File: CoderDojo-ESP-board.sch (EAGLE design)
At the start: 17 parts, among them IC1 ESP-12E/F, IC2 FT232RL, X1 PN61729-S

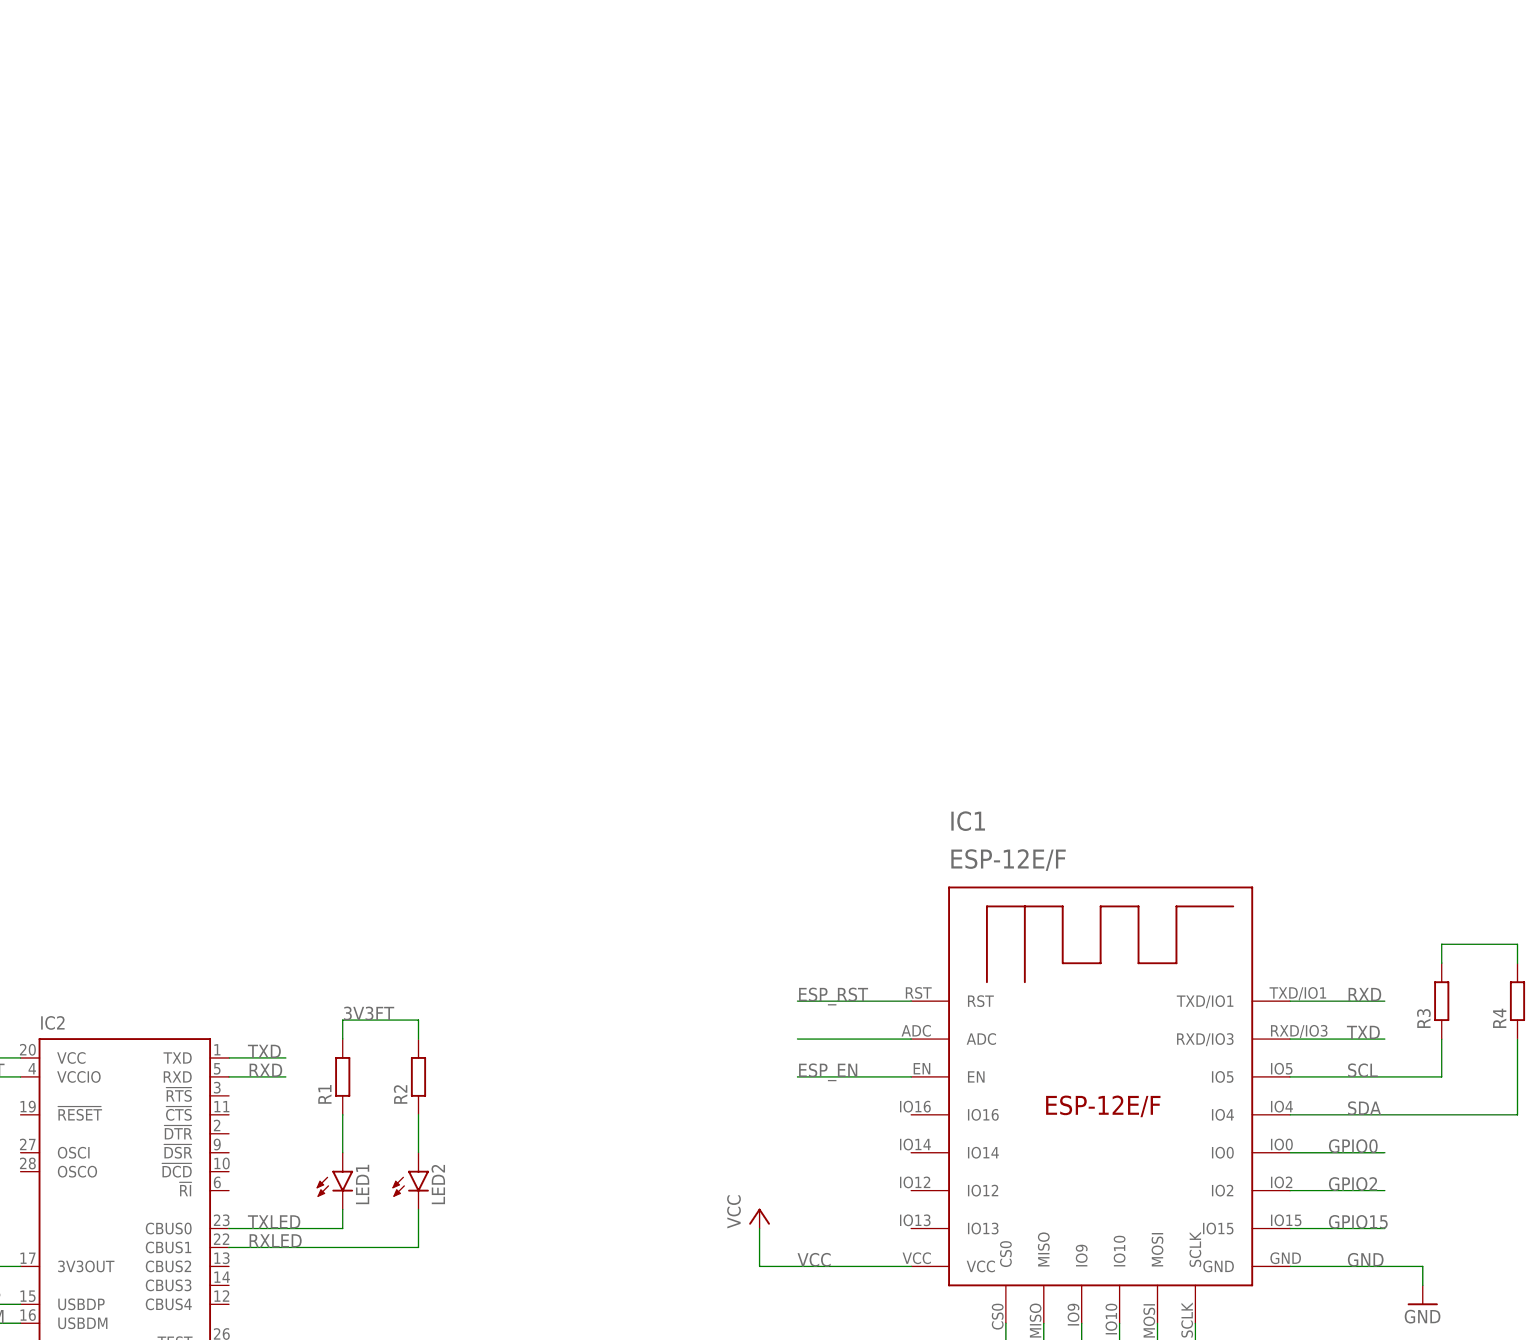
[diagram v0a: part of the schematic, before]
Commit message: Add PCA9685PW library + add to schematic
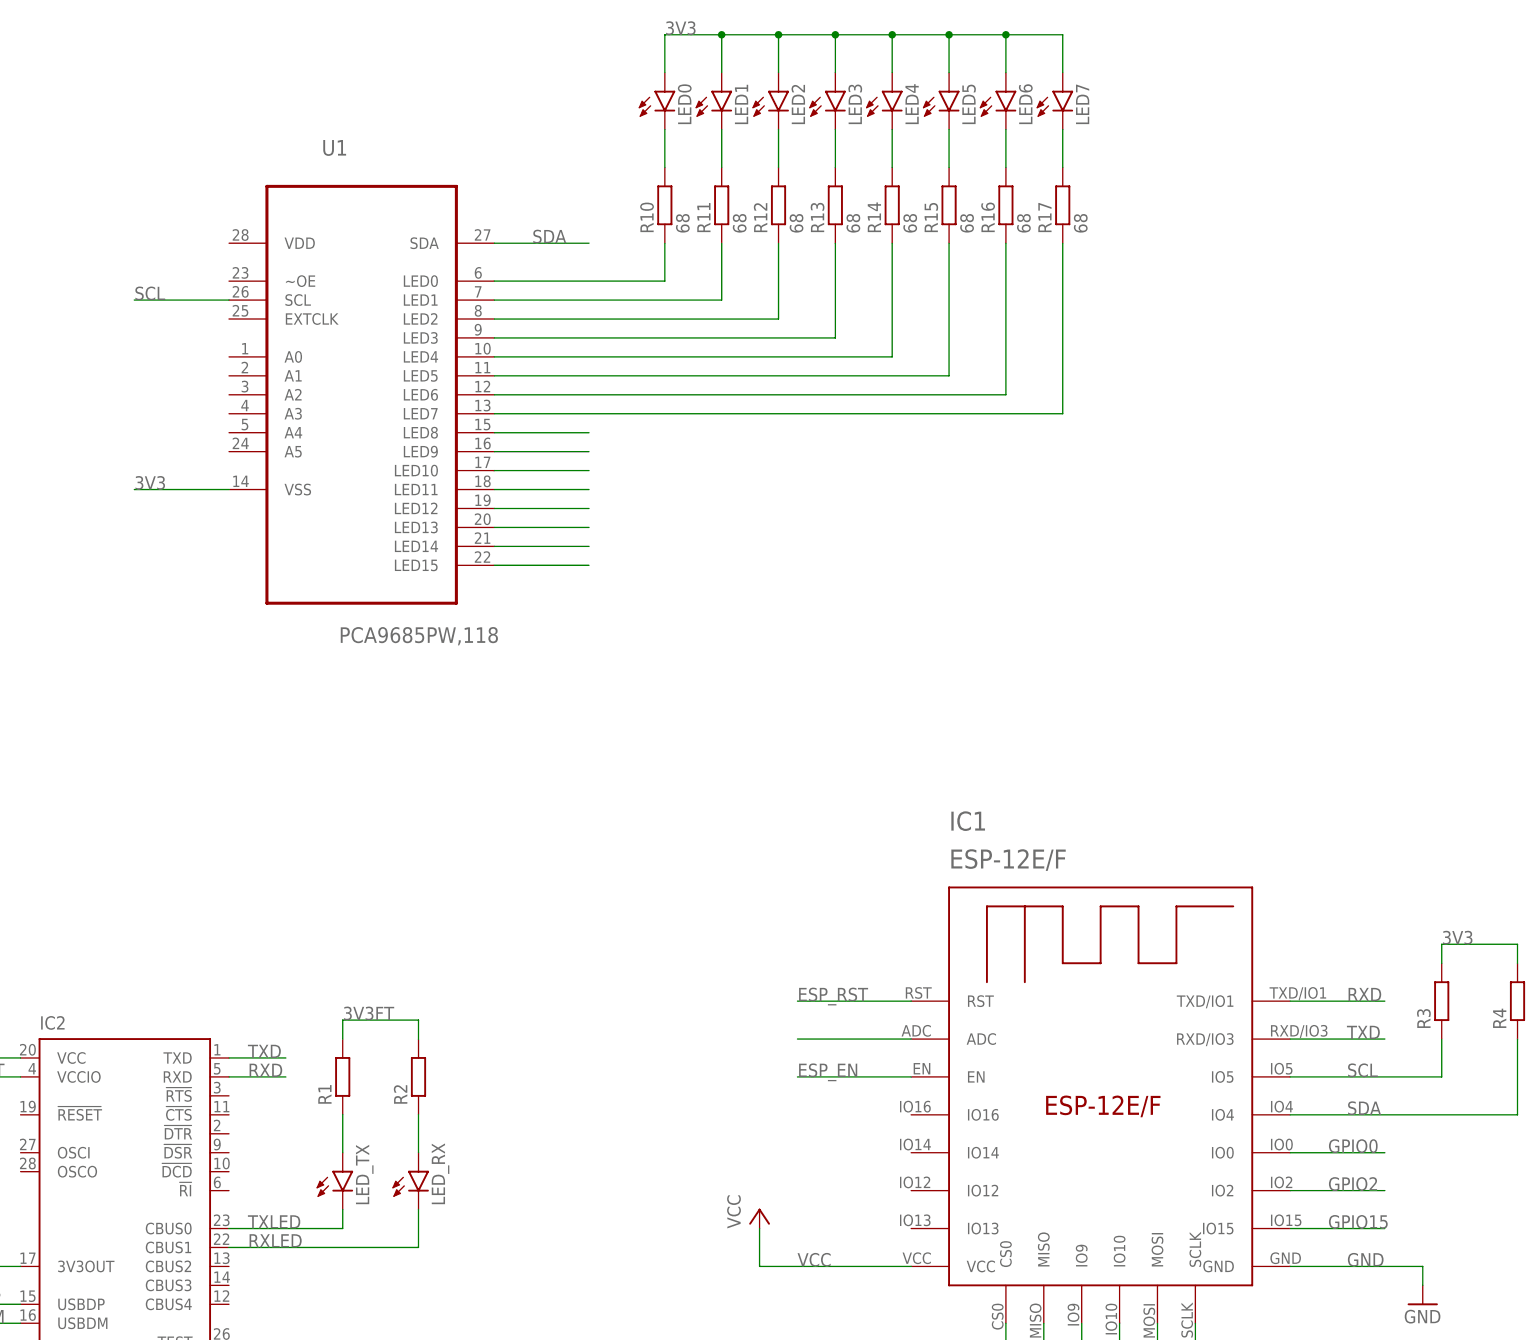
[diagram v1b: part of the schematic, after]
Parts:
- added LED0, LED3, LED4, LED5, LED6, LED7: (no value), led:LED3MM
- added LED_RX, LED_TX: (no value), led:LEDSML0805
- added R10, R11, R12, R13, R14, R15, R16, R17: 68, rcl:R-EU_R0805
- added U1: PCA9685PW,118, PCA9685PW_118:PCA9685PW,118
- LED1, LED2: device led:LEDSML0805 -> led:LED3MM
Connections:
- removed net N$10: R3.2, R4.2
- new net N$15: R15.1, U1.LED5
- new net N$16: R16.1, U1.LED6
- new net N$18: R17.1, U1.LED7
- new net N$19: U1.LED8
- new net N$20: U1.LED9
- new net N$21: U1.LED10
- new net N$22: U1.LED11
- new net N$23: U1.LED12
- new net N$24: U1.LED13
- new net N$25: U1.LED14
- new net N$26: U1.LED15
- new net N$27: LED0.C, R10.2
- new net N$28: LED1.C, R11.2
- new net N$29: LED2.C, R12.2
- new net N$30: LED3.C, R13.2
- new net N$31: LED4.C, R14.2
- new net N$32: LED5.C, R15.2
- new net N$33: LED6.C, R16.2
- new net N$34: LED7.C, R17.2
- new net N$4: R10.1, U1.LED0
- new net N$5: R11.1, U1.LED1
- new net N$6: R12.1, U1.LED2
- new net N$7: R13.1, U1.LED3
- new net N$8: R14.1, U1.LED4
- net 3V3: now also LED0.A, LED1.A, LED2.A, LED3.A, LED4.A, LED5.A, LED6.A, LED7.A, R3.2, R4.2, U1.VSS
- net N$1: now also LED_TX.A; no longer LED1.A
- net N$2: now also LED_RX.A; no longer LED2.A
- net RXLED: now also LED_RX.C; no longer LED2.C
- net SCL: now also U1.SCL
- net SDA: now also U1.SDA
- net TXLED: now also LED_TX.C; no longer LED1.C
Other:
- moved on the sheet: LED1, LED2

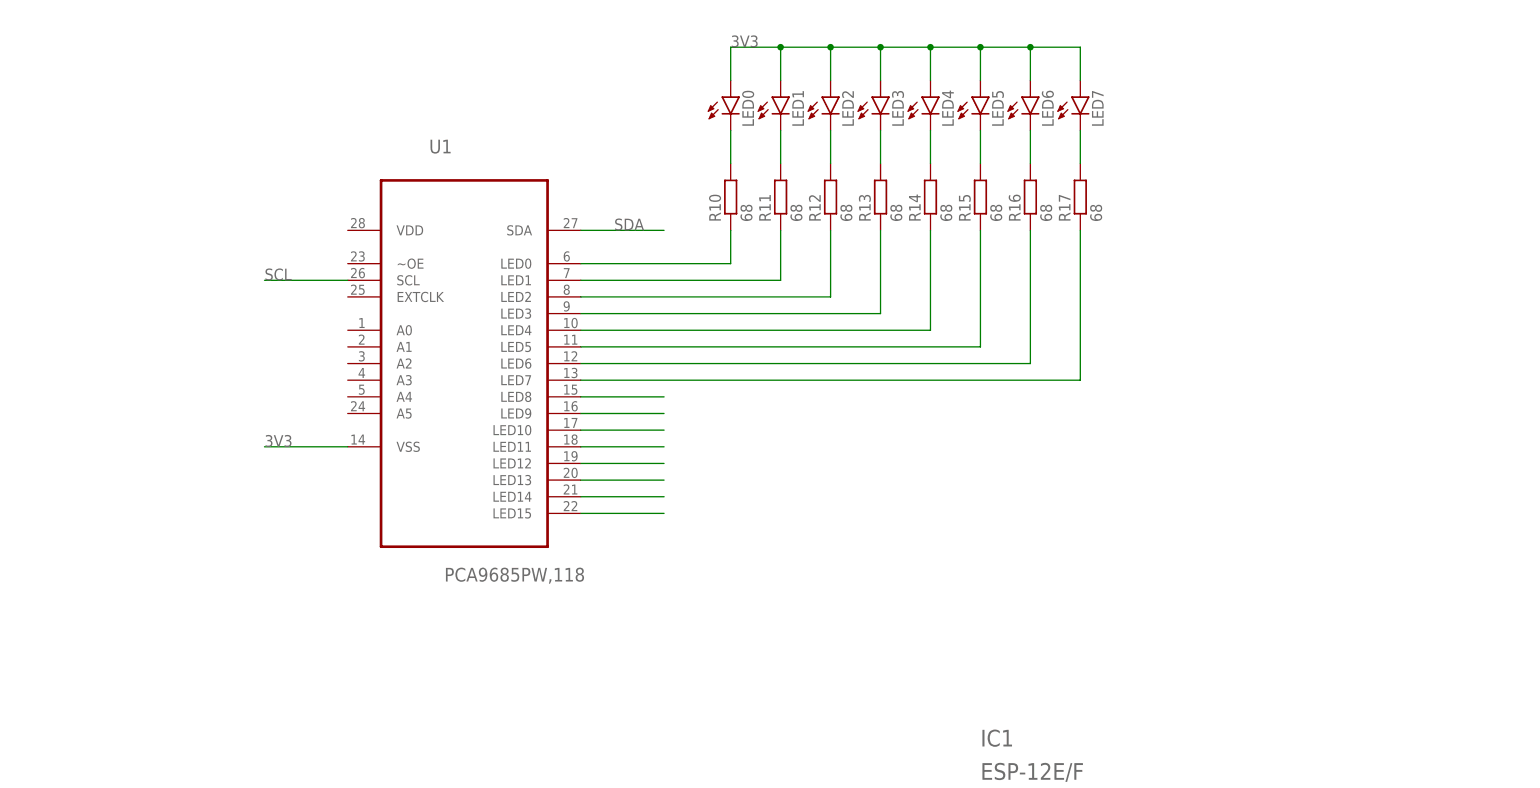
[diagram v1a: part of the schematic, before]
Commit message: change AMS1117 library + add to schematic
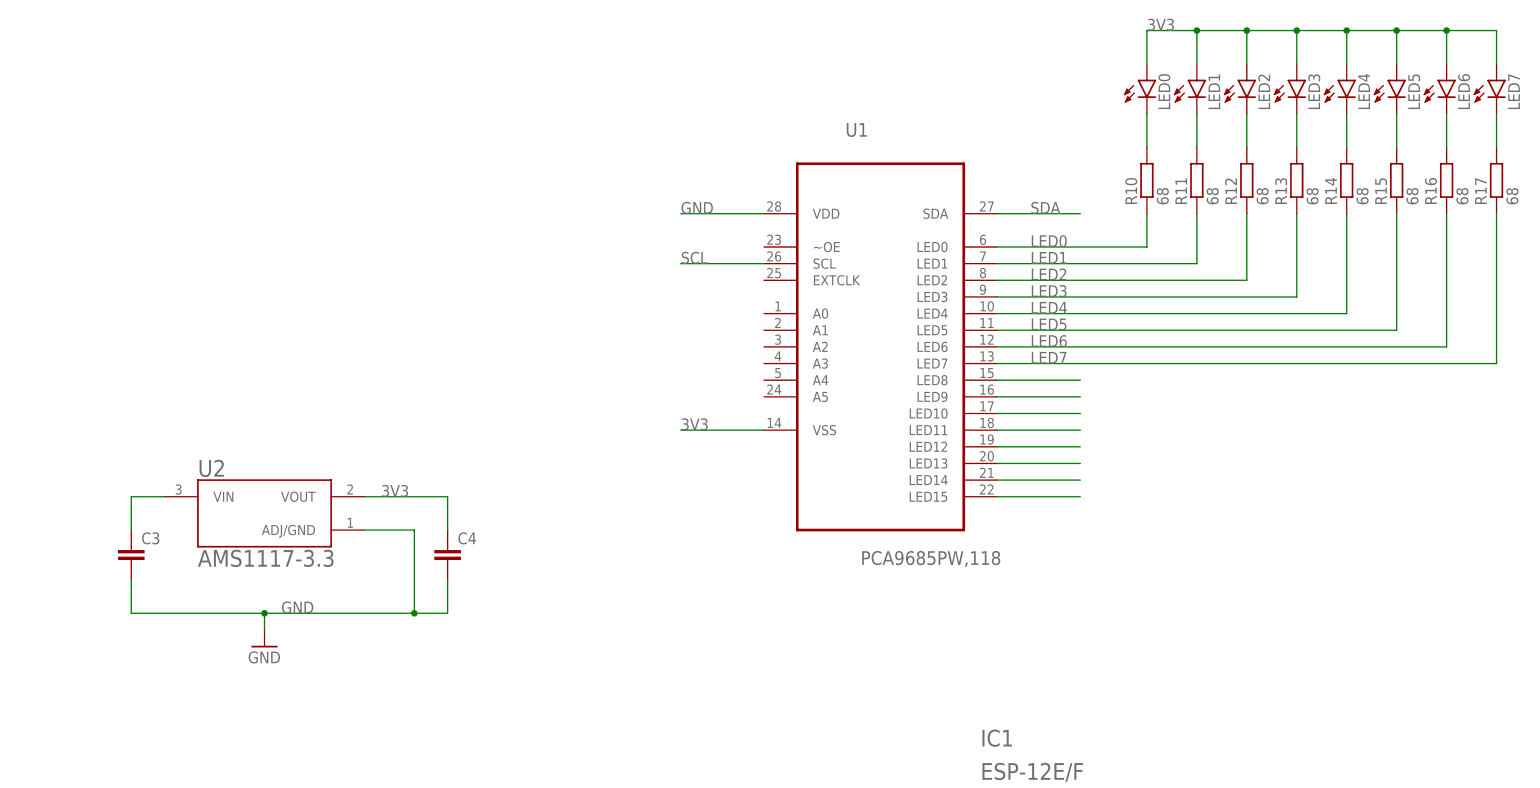
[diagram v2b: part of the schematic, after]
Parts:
- added C3, C4: (no value), rcl:C-EUC0805
- added U2: AMS1117-3.3, AMS1117-3.3:AMS1117-3.3
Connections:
- net N$15 renamed LED5
- net N$16 renamed LED6
- net N$18 renamed LED7
- net N$4 renamed LED0
- net N$5 renamed LED1
- net N$6 renamed LED2
- net N$7 renamed LED3
- net N$8 renamed LED4
- new net N$35: C3.1, U2.VIN
- net 3V3: now also C4.1, U2.VOUT
- net GND: now also C3.2, C4.2, U1.VDD, U2.ADJ/GND
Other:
- moved on the sheet: LED0, LED1, LED2, LED3, LED4, LED5, LED6, LED7, R10, R11, R12, R13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
